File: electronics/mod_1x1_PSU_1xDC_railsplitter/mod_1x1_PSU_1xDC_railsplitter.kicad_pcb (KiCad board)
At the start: 2 copper layers, 42.5 x 46.2 mm, 11 parts, among them J1 module_2x15_left_input, J2 module_2x15_right_input, J3 Jack-DC, J5 Conn_01x02

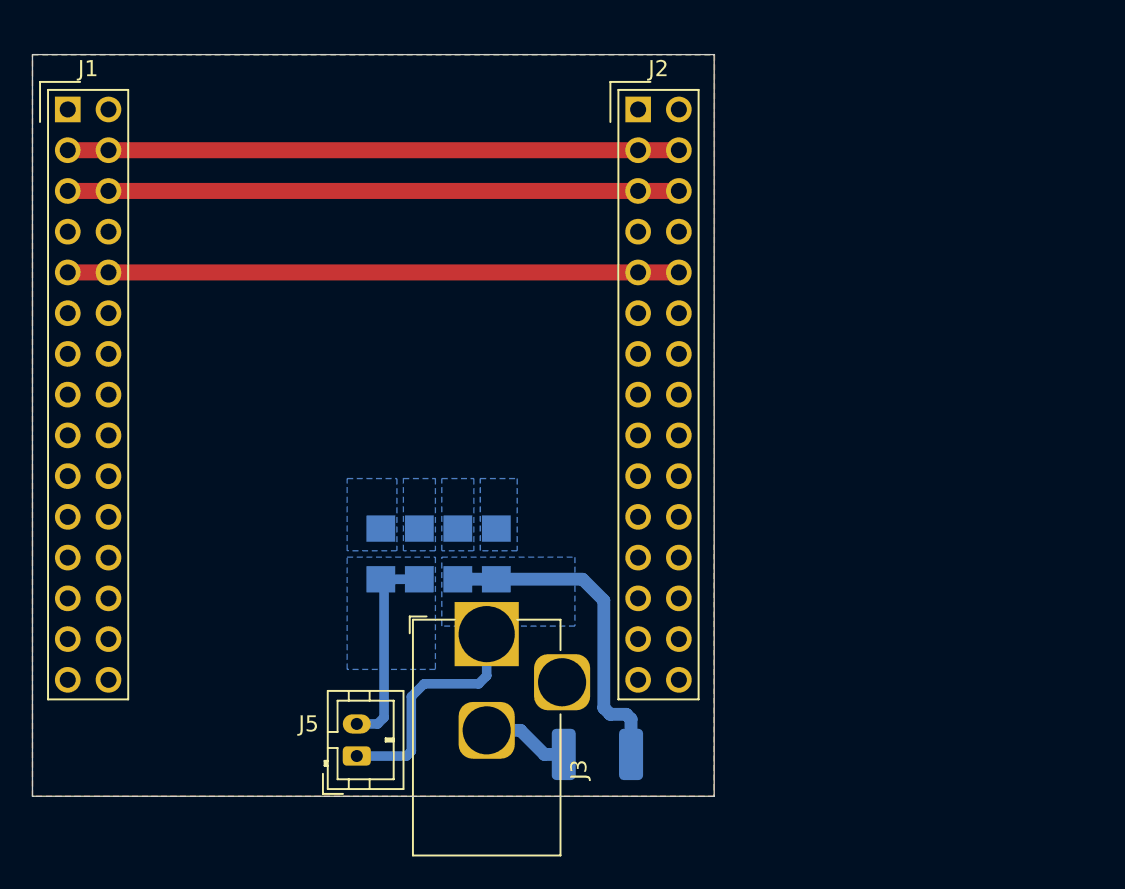
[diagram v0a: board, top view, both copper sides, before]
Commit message: WIP initial LDO schematic, updated PCB library
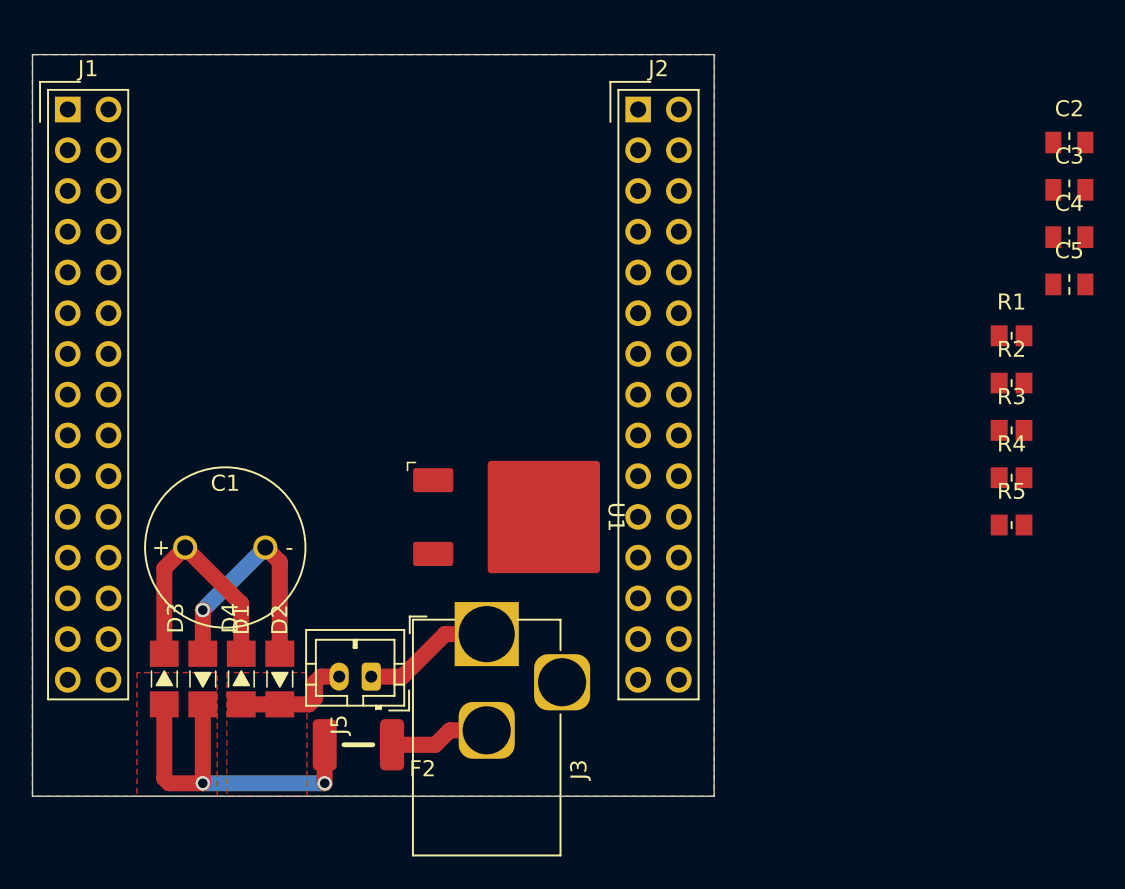
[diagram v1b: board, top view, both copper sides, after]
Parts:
- added C1: 100u, SquantorRcl:C-050-100-elco, F.Cu at (154.6, 99.7)
- added C2: 10u, SquantorRcl:C_0805, F.Cu at (207.2, 74.5)
- added C3: 10u, SquantorRcl:C_0805, F.Cu at (207.2, 77.4)
- added C4: 10u, SquantorRcl:C_0805, F.Cu at (207.2, 80.3)
- added C5: 10u, SquantorRcl:C_0805, F.Cu at (207.2, 83.3)
- added R1: 1, SquantorRcl:R_0805+0603, F.Cu at (203.6, 86.5)
- added R2: 120, SquantorRcl:R_0805+0603, F.Cu at (203.6, 89.5)
- added R3: ADJ, SquantorRcl:R_0805+0603, F.Cu at (203.6, 92.4)
- added R4: ADJ, SquantorRcl:R_0805+0603, F.Cu at (203.6, 95.3)
- added R5: ADJ, SquantorRcl:R_0805+0603, F.Cu at (203.6, 98.3)
- added U1: ~, SquantorIC:TO-252_D-PAK_IRF, F.Cu at (174.5, 97.8)
- D1, D2, D3, D4, F2: moved to F.Cu
- moved D4 19.9 mm to (153.2, 107.9)
- moved D3 19.9 mm to (150.8, 107.9)
- moved F2 14.9 mm to (162.9, 112.0), turned to 180 degrees
- moved D1 11.7 mm to (155.6, 107.9)
- moved D2 11.7 mm to (158.0, 107.9)
- moved J5 5.03 mm to (163.7, 107.8), turned to 180 degrees
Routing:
- net /V-A: track 38.1 -> 0.00 mm
- net /V+A: track 38.1 -> 0.00 mm
- net /+5V: track 38.1 -> 0.00 mm
- net /DC1n: track 0.00 -> 15.2 mm, vias 0 -> 1
- net /DC1p: track 0.00 -> 15.2 mm
- net /AC1_PHASE_IN: track 14.8 -> 8.30 mm
- net /AC1_PHASE: track 13.0 -> 7.40 mm
- net /AC1_NEUT: track 20.5 -> 22.1 mm, vias 0 -> 2
- net Net-(F2-Pad1): track 5.42 -> 6.27 mm
- added copper zone on F.Cu, net /AC1_NEUT
- added copper zone on F.Cu, net /AC1_PHASE
- removed copper zone on B.Cu, net /AC1_NEUT
- removed copper zone on B.Cu, net /AC1_PHASE
- removed copper zone on B.Cu, net /DC1n
- removed copper zone on B.Cu, net /DC1p

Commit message: WIP schematic entry
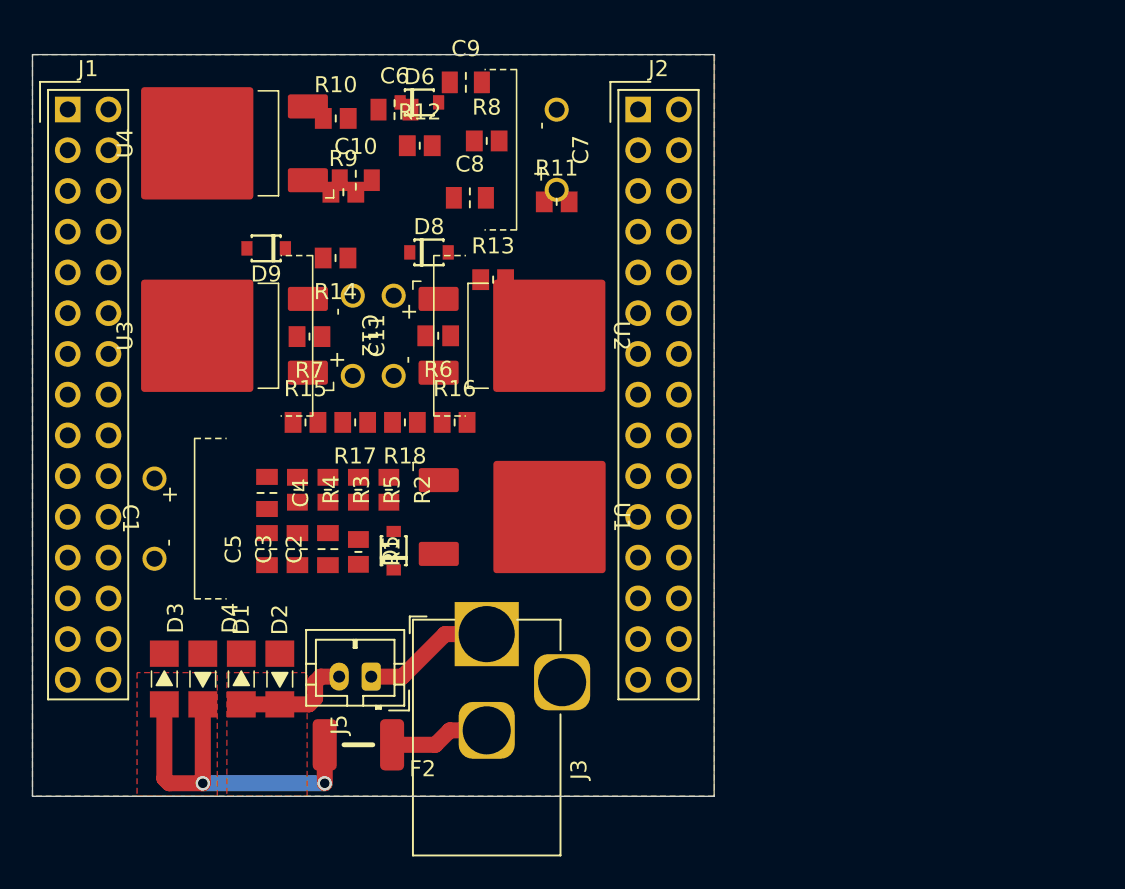
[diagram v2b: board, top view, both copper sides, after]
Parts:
- added C10: 10u, SquantorRcl:C_0805, F.Cu at (162.7, 76.8)
- added C11: 100u, SquantorRcl:C-050-100-elco-lying, F.Cu at (162.6, 86.5)
- added C12: 100u, SquantorRcl:C-050-100-elco-lying, F.Cu at (165.1, 86.5)
- added C6: 10u, SquantorRcl:C_0805, F.Cu at (165.2, 72.4)
- added C7: 100u, SquantorRcl:C-050-100-elco-lying, F.Cu at (175.3, 74.9)
- added C8: 10u, SquantorRcl:C_0805, F.Cu at (169.8, 77.9)
- added C9: 10u, SquantorRcl:C_0805, F.Cu at (169.6, 70.7)
- added D5: D, SquantorDiodes:SOD-323-onsemi, F.Cu at (165.1, 99.9)
- added D6: D, SquantorDiodes:SOD-323-onsemi, F.Cu at (166.7, 72.0)
- added D8: D, SquantorDiodes:SOD-323-onsemi, F.Cu at (167.3, 81.3)
- added D9: D, SquantorDiodes:SOD-323-onsemi, F.Cu at (157.2, 81.0)
- added R10: ADJ, SquantorRcl:R_0805+0603, F.Cu at (161.5, 73.0)
- added R11: 120, SquantorRcl:R_0805+0603, F.Cu at (175.3, 78.2)
- added R12: 1, SquantorRcl:R_0805+0603, F.Cu at (166.7, 74.7)
- added R13: 1, SquantorRcl:R_0805+0603, F.Cu at (171.3, 83.0)
- added R14: 1, SquantorRcl:R_0805+0603, F.Cu at (161.5, 81.7)
- added R15: 1K, SquantorRcl:R_0805+0603, F.Cu at (159.6, 91.9)
- added R16: 1K, SquantorRcl:R_0805+0603, F.Cu at (168.9, 91.9)
- added R17: 10K, SquantorRcl:R_0805+0603, F.Cu at (162.7, 91.9)
- added R18: 10K, SquantorRcl:R_0805+0603, F.Cu at (165.8, 91.9)
- added R6: 120, SquantorRcl:R_0805+0603, F.Cu at (167.9, 86.5)
- added R7: 120, SquantorRcl:R_0805+0603, F.Cu at (159.8, 86.5)
- added R8: ADJ, SquantorRcl:R_0805+0603, F.Cu at (170.9, 74.3)
- added R9: ADJ, SquantorRcl:R_0805+0603, F.Cu at (162.0, 77.5)
- added U2: LM317, SquantorIC:TO-252_D-PAK_IRF, F.Cu at (174.8, 86.5)
- added U3: LM337, SquantorIC:TO-252_D-PAK_IRF, F.Cu at (152.8, 86.5)
- added U4: LD1117, SquantorIC:TO-252_D-PAK_IRF, F.Cu at (152.8, 74.5)
- C1: footprint SquantorRcl:C-050-100-elco -> SquantorRcl:C-050-100-elco-lying
- U1: value ~ -> LD1117
- moved C3 53.1 mm to (159.1, 99.8), turned to 90 degrees
- moved C2 52.7 mm to (161.0, 99.8), turned to 90 degrees
- moved C5 52.7 mm to (157.2, 99.8), turned to 90 degrees
- moved C4 52.5 mm to (157.2, 96.3), turned to -90 degrees
- moved R4 44.5 mm to (159.1, 96.1), turned to -90 degrees
- moved R1 42.9 mm to (162.9, 100.0), turned to -90 degrees
- moved R3 42.8 mm to (161.0, 96.1), turned to -90 degrees
- moved R5 40.8 mm to (162.9, 96.1), turned to -90 degrees
- moved R2 39.4 mm to (164.8, 96.1), turned to -90 degrees
- moved C1 4.77 mm to (150.2, 97.9), turned to -90 degrees
- moved N2 1.10 mm to (167.4, 87.8)
- moved U1 0.35 mm to (174.8, 97.8)
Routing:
- net /DC1n: track 15.2 -> 0.00 mm, vias 1 -> 0
- net /DC1p: track 15.2 -> 0.00 mm

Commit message: small schematic updates and place and route
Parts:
- added RV1: 1K, Potentiometer_THT:Potentiometer_Bourns_3386P_Vertical, F.Cu at (161.4, 90.4)
- C1: footprint SquantorRcl:C-050-100-elco-lying -> SquantorRcl:C-050-100-elco-lying_flip
- N1: value 202200917 -> 20230924
- moved C7 24.9 mm to (150.4, 74.4), turned to -90 degrees
- moved U4 21.8 mm to (174.7, 74.5), turned to -90 degrees
- moved R8 12.0 mm to (159.0, 72.7), turned to 90 degrees
- moved R11 11.9 mm to (164.7, 72.7), turned to 90 degrees
- moved C9 11.9 mm to (159.0, 76.0), turned to 90 degrees
- moved C8 9.15 mm to (160.9, 76.0), turned to 90 degrees
- moved R9 6.87 mm to (157.1, 72.7), turned to 90 degrees
- moved C10 5.69 mm to (157.1, 76.0), turned to 90 degrees
- moved R5 5.25 mm to (157.7, 96.8), turned to 90 degrees
- moved R3 5.25 mm to (155.8, 96.8), turned to 90 degrees
- moved R4 5.25 mm to (153.9, 96.8), turned to 90 degrees
- moved D6 4.58 mm to (165.0, 76.2), turned to 90 degrees
- moved R12 4.22 mm to (162.8, 76.2), turned to -90 degrees
- moved U1 3.42 mm to (171.5, 98.5)
- moved D5 3.37 mm to (161.8, 100.3)
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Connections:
- C6 pad 1: Net-(C6-Pad1) -> GND
- R17 pad 1: unconnected-(R17-Pad1) -> Net-(R15-Pad2)
- R17 pad 2: Net-(R15-Pad2) -> Net-(R17-Pad2)
- R18 pad 2: unconnected-(R18-Pad2) -> Net-(R18-Pad2)
- R8 pad 1: Net-(C6-Pad1) -> GND
- R9 pad 1: Net-(C6-Pad1) -> GND
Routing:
- net /DC1n: track 0.00 -> 40.6 mm, vias 0 -> 2
- net /DC1p: track 0.00 -> 26.7 mm
- net Net-(U4-ADJ/GND): track 0.00 -> 8.42 mm
- net Net-(U1-ADJ/GND): track 0.00 -> 8.39 mm
- net VDD: track 0.00 -> 8.37 mm, vias 0 -> 22
- net Net-(C10-Pad1): track 0.00 -> 5.71 mm
- net Net-(C2-Pad1): track 0.00 -> 5.71 mm
- net Net-(R10-Pad2): track 0.00 -> 3.80 mm
- net Net-(R3-Pad2): track 0.00 -> 3.80 mm
- net /+5V: track 0.00 -> 2.38 mm, vias 0 -> 22
- added copper zone on B.Cu, net /+5V
- added copper zone on F.Cu, net /+5V
- added copper zone on B.Cu, net VDD
- added copper zone on F.Cu, net VDD

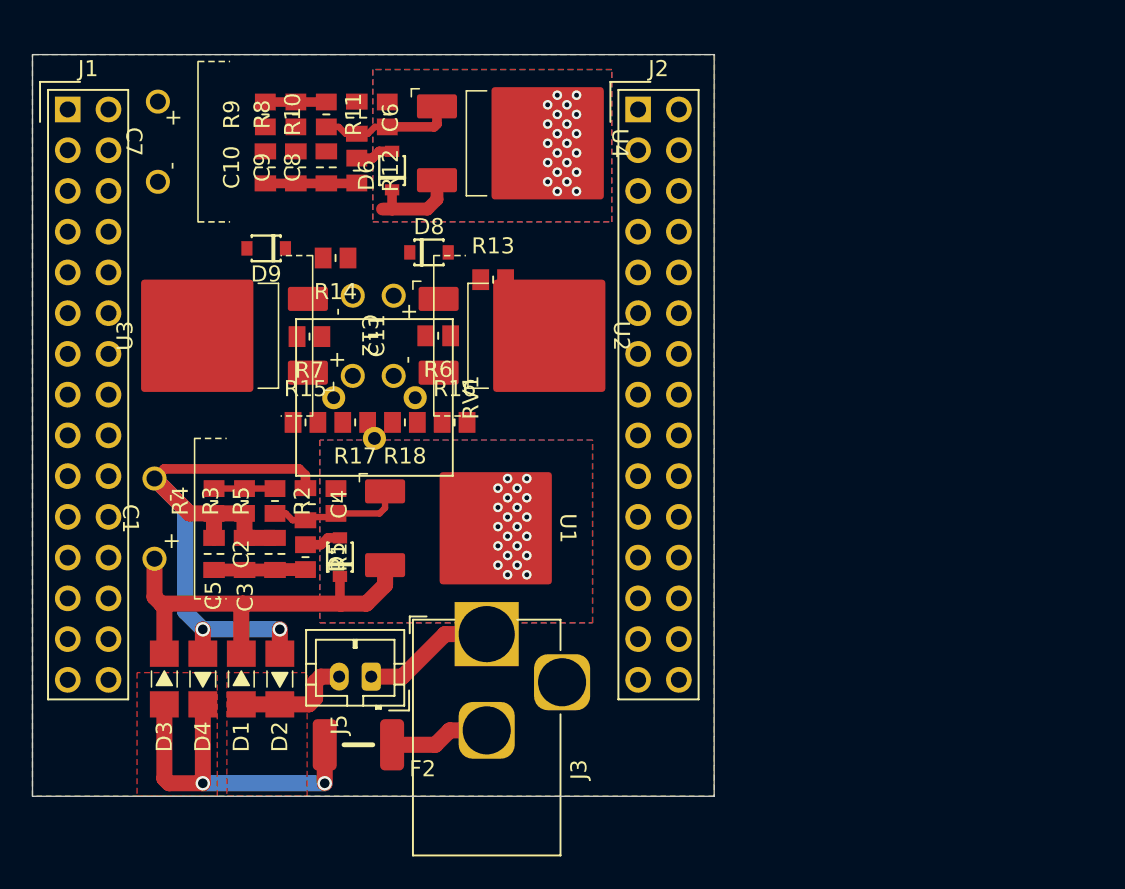
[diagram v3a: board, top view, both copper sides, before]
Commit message: WIP placement, done schematic
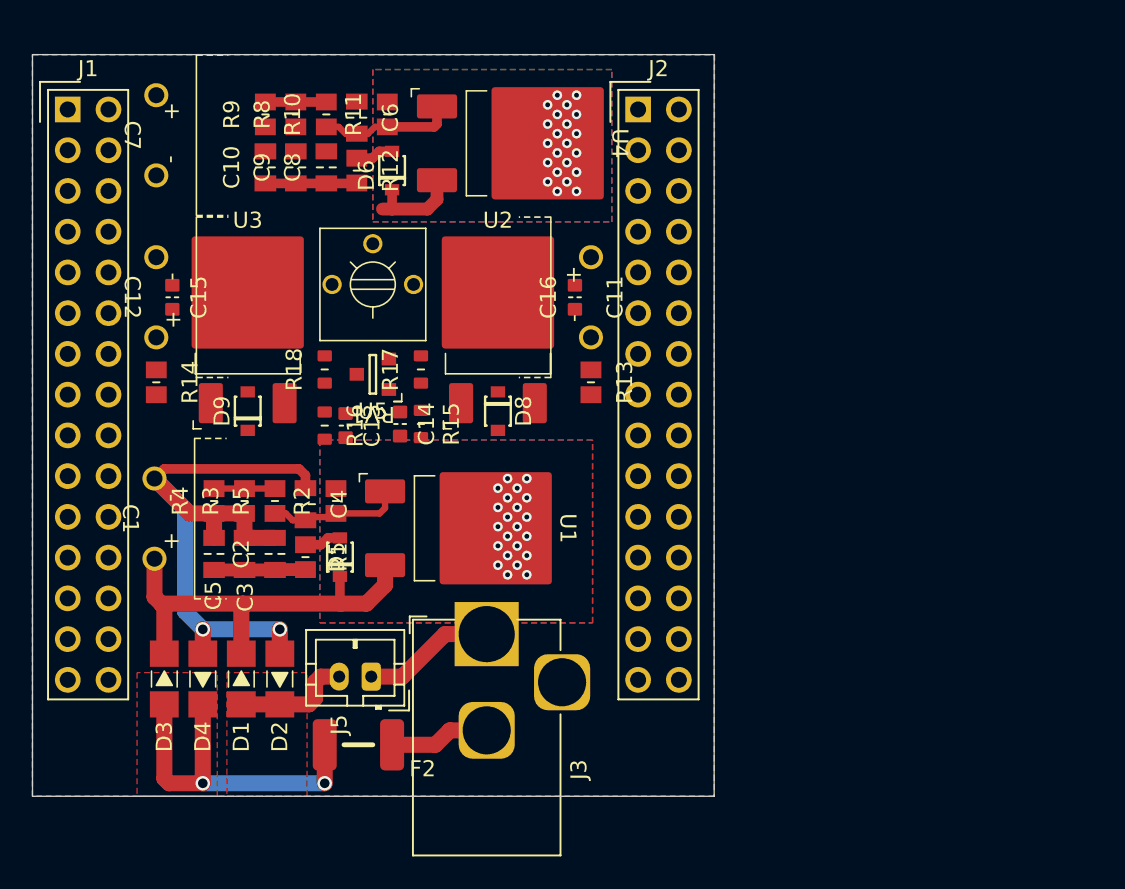
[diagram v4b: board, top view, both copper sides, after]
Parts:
- removed R6, R7: 120, SquantorRcl:R_0805+0603
- added C13: 10u, SquantorRcl:C_0603, F.Cu at (162.1, 92.1)
- added C14: 10u, SquantorRcl:C_0603, F.Cu at (165.5, 92.0)
- added C15: 10u, SquantorRcl:C_0603, F.Cu at (151.3, 84.1)
- added C16: 10u, SquantorRcl:C_0603, F.Cu at (176.4, 84.1)
- added U5: TLV431, SquantorIC:SOT23-3, F.Cu at (163.8, 88.9)
- C11, C12: footprint SquantorRcl:C-050-100-elco-lying -> SquantorRcl:C-050-100-elco-lying_flip
- R15, R16, R17, R18: footprint SquantorRcl:R_0805+0603 -> SquantorRcl:R_0603_hand
- RV1: footprint Potentiometer_THT:Potentiometer_Bourns_3386P_Vertical -> SquantorRcl:POT-Bourns-3362P
- moved N2 31.5 mm to (198.9, 86.6)
- moved C11 15.0 mm to (177.4, 84.1)
- moved C12 15.0 mm to (150.3, 84.1)
- moved R14 13.6 mm to (150.3, 89.4), turned to -90 degrees
- moved D8 10.8 mm to (171.6, 91.2), turned to -90 degrees
- moved D9 10.2 mm to (156.0, 91.2), turned to 90 degrees
- moved R13 8.84 mm to (177.4, 89.4), turned to -90 degrees
- moved R16 8.10 mm to (160.8, 92.1), turned to -90 degrees
- moved RV1 7.47 mm to (163.8, 83.3), turned to 180 degrees
- moved R15 7.20 mm to (166.8, 92.0), turned to -90 degrees
- moved R18 5.99 mm to (160.8, 88.6), turned to 90 degrees
- moved R17 5.26 mm to (166.8, 88.6), turned to 90 degrees
- moved U2 4.19 mm to (171.6, 83.8), turned to 0 degrees
- moved U3 4.15 mm to (156.0, 83.8), turned to 0 degrees
- moved C7 0.41 mm to (150.3, 74.0)
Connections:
- D8 pad 1: VDD -> Net-(D8-K)
- D9 pad 2: /DC1n -> Net-(D9-A)
- R13 pad 2: Net-(D8-A) -> Net-(D8-K)
- R14 pad 2: Net-(D9-K) -> Net-(D9-A)
- R15 pad 1: VDD -> Net-(D8-A)
- R15 pad 2: Net-(R15-Pad2) -> VDD
- R16 pad 1: Net-(R16-Pad1) -> Net-(D9-K)
- R17 pad 1: Net-(R15-Pad2) -> Net-(D8-A)
- R18 pad 1: Net-(R16-Pad1) -> Net-(D9-K)
- RV1 pad 2: unconnected-(RV1-Pad2) -> Net-(U5-REF)
- U2 pad 1: Net-(U2-ADJ) -> Net-(D8-A)
- U2 pad 2: Net-(D8-A) -> Net-(D8-K)
- U3 pad 1: Net-(U3-ADJ) -> Net-(D9-K)
- U3 pad 3: Net-(D9-K) -> Net-(D9-A)
